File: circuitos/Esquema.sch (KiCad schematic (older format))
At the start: 8 parts, among them U1 LM311N

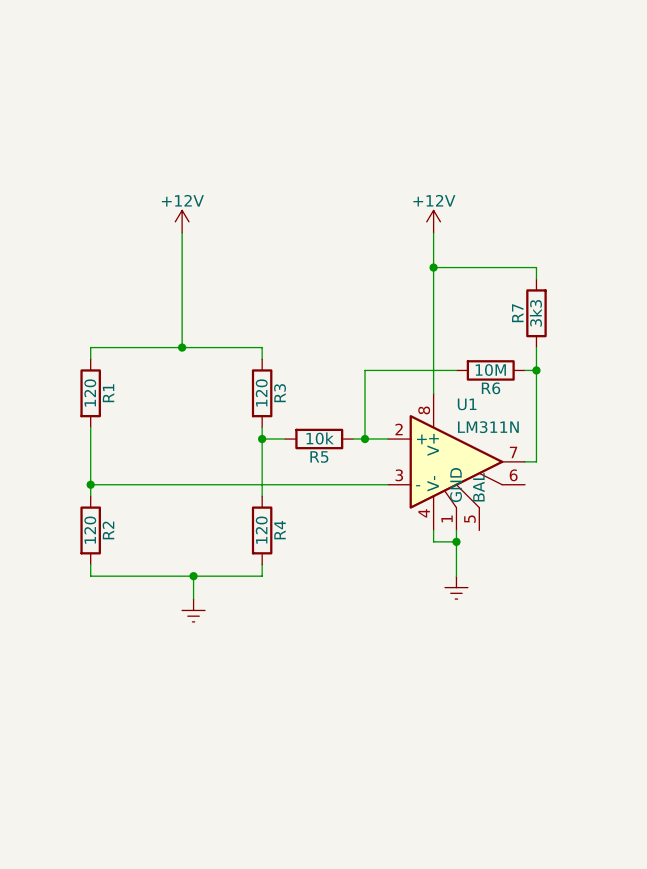
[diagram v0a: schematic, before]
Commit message: Revisão do circuito com dois comparadores e LEDs. Ainda há ajustes a realizar.
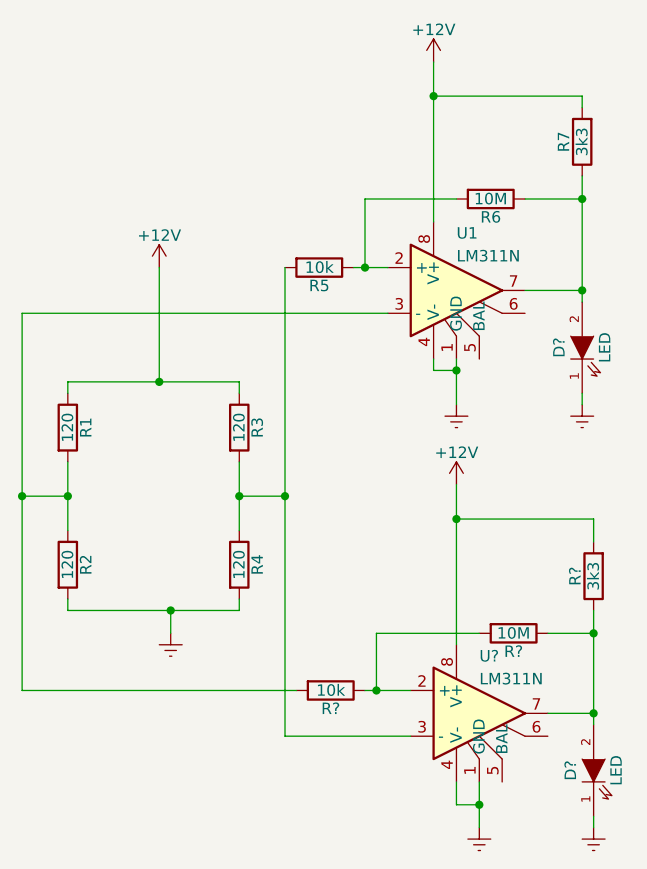
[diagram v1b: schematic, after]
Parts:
- added D? (x2): LED, symbol LED
- added R?: 3k3, symbol R
- added R?: 10M, symbol R
- added R?: 10k, symbol R
- added U?: LM311N, symbol LM311N
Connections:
- net +12V: now also R?.2, U?.8 (V+)
- net Earth: now also D?.1 (K), D?.1 (K), U?.1 (GND), U?.4 (V-)
- net at R1.2, R2.1, U1.3 (-): now also R?.2
- net at R3.2, R4.1, R5.2: now also U?.3 (-)
- net at R6.1, R7.1, U1.7: now also D?.2 (A)
- new net: R?.1, R?.2, U?.2 (+)
- new net: D?.2 (A), R?.1, R?.1, U?.7
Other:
- moved on the sheet: R1, R2, R3, R4, R5, R6, R7, U1
